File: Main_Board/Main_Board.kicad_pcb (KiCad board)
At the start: 2 copper layers, 60 x 50 mm, 26 parts, among them J1 USB_C_Receptacle_USB2.0_16P, J2 Conn_01x04_Pin, J4 Conn_01x03_Pin, J5 Conn_01x03_Pin, Q1 NMOS, U1 DEV-15583, U2 XIAO-ESP32-C3-DIP, U4 NE555D, U5 TPS72101DBVR

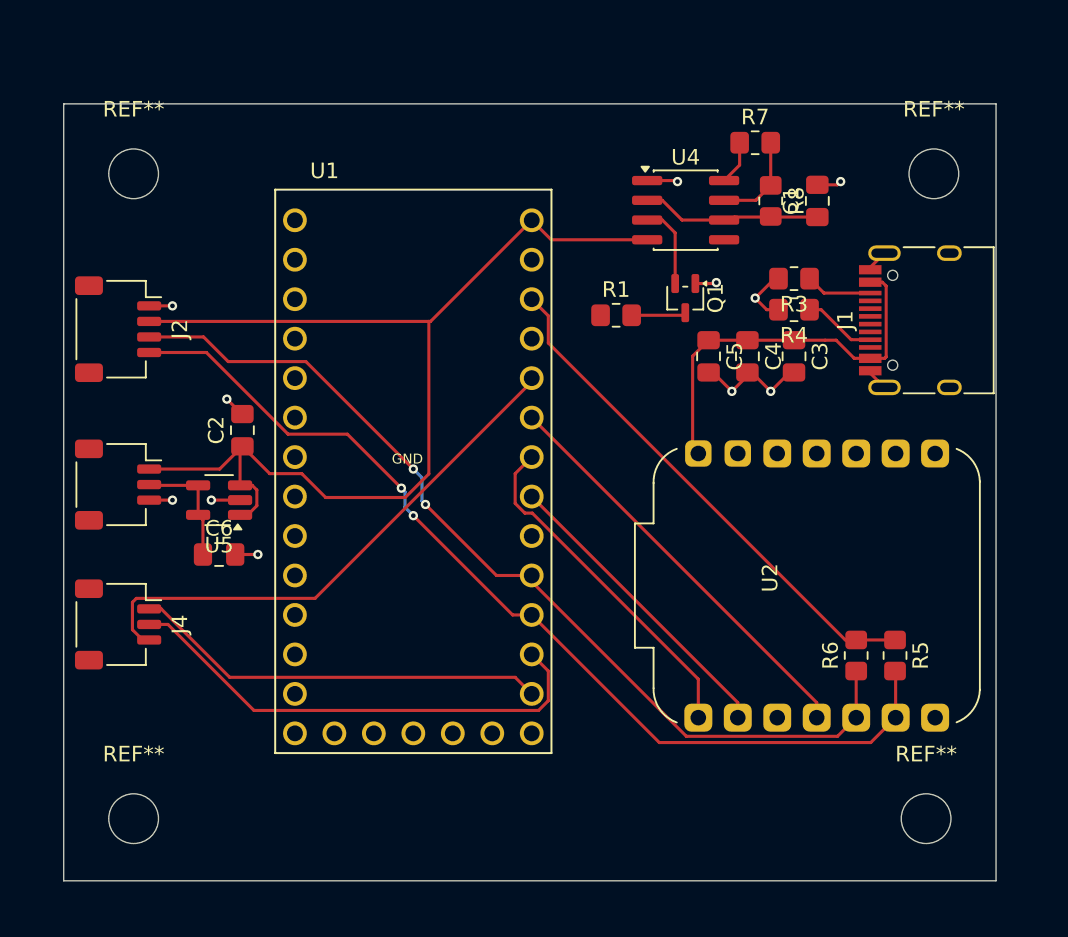
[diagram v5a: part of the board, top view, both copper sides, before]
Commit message: moved mounting holes
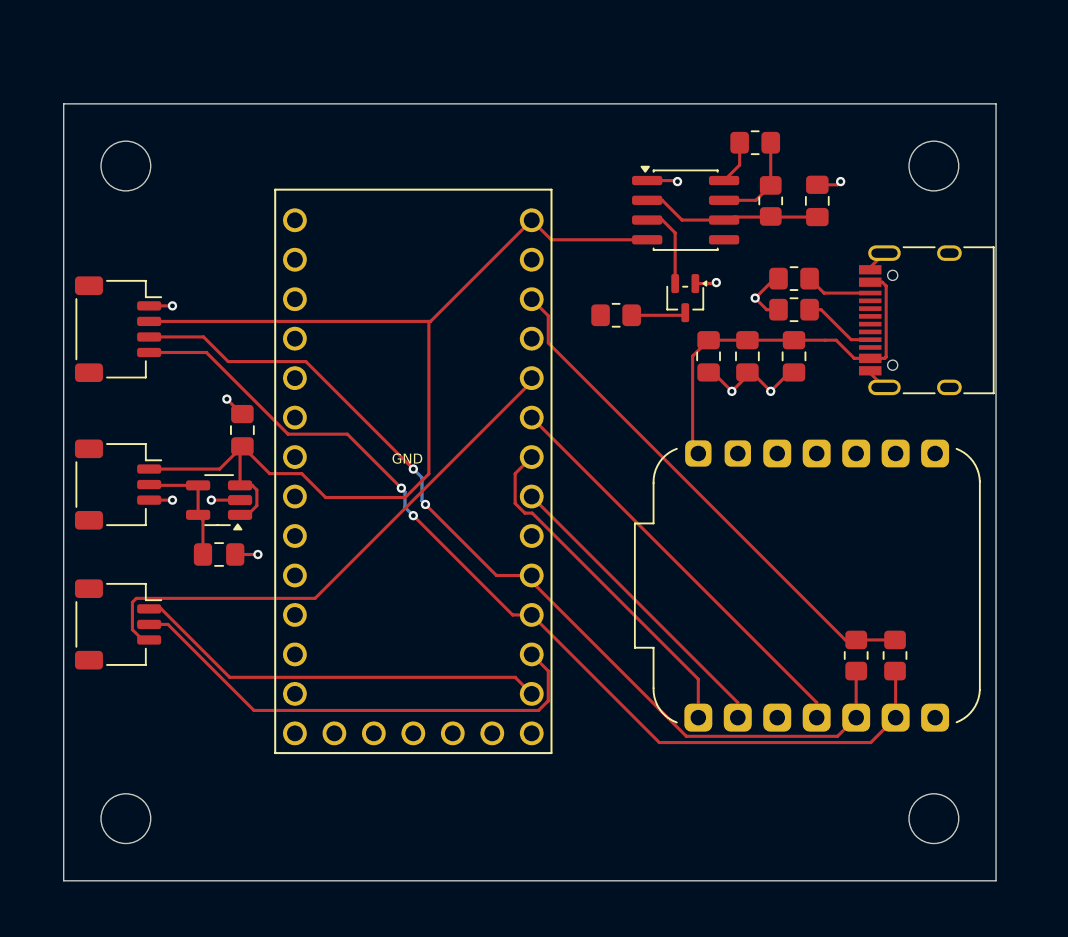
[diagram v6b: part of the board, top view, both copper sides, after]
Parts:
- moved REF** 0.71 mm to (74.0, 79.5)
- moved REF** 0.50 mm to (74.0, 121.5)
- moved REF** 0.50 mm to (126.0, 79.5)
- moved REF** 0.50 mm to (126.0, 121.5)
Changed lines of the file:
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@@
 			(outputformat 1)
 			(mirror no)
-			(drillshape 1)
+			(drillshape 0)
 			(scaleselection 1)
-			(outputdirectory "")
+			(outputdirectory "C:/Users/Maana/Downloads/Feb17_TN_Gerbs/")
 		)
 	)
@@
 			(at 0 -1.68 0)
 			(layer "F.SilkS")
+			(hide yes)
 			(effects
 				(font
@@
 			(at -5.715 -19.685 0)
 			(layer "F.SilkS")
+			(hide yes)
 			(effects
 				(font
@@
 			(at 0 -1.68 90)
 			(layer "F.SilkS")
+			(hide yes)
 			(effects
 				(font
@@
 	(footprint "MountingHole:MountingHole_3.2mm_M3"
 		(layer "F.Cu")
-		(at 74.5 80)
+		(at 74 79.5)
 		(descr "Mounting Hole 3.2mm, M3, no annular, generated by kicad-footprint-generator mountinghole.py")
 		(tags "mountinghole M3")
@@
 			(at 0 -4.15 0)
 			(layer "F.SilkS")
+			(hide yes)
 			(effects
 				(font
@@
 			(at 0 -5.645 90)
 			(layer "F.SilkS")
+			(hide yes)
 			(effects
 				(font
@@
 			(at 0 -1.65 90)
 			(layer "F.SilkS")
+			(hide yes)
 			(effects
 				(font
@@
 			(at 0 -1.65 90)
 			(layer "F.SilkS")
+			(hide yes)
 			(effects
 				(font
@@
 	(footprint "MountingHole:MountingHole_3.2mm_M3"
 		(layer "F.Cu")
-		(at 74.5 121.5)
+		(at 74 121.5)
 		(descr "Mounting Hole 3.2mm, M3, no annular, generated by kicad-footprint-generator mountinghole.py")
 		(tags "mountinghole M3")
@@
 			(at 0 -4.15 0)
 			(layer "F.SilkS")
+			(hide yes)
 			(effects
 				(font
@@
 			(unlocked yes)
 			(layer "F.SilkS")
+			(hide yes)
 			(effects
 				(font
@@
 			(at 0 -2.9 0)
 			(layer "F.SilkS")
+			(hide yes)
 			(effects
 				(font
@@
 			(at 0 -3.98 90)
 			(layer "F.SilkS")
+			(hide yes)
 			(effects
 				(font
@@
 			(at 0 -3.4 0)
 			(layer "F.SilkS")
+			(hide yes)
 			(effects
 				(font
@@
 			(at 0 -3.98 90)
 			(layer "F.SilkS")
+			(hide yes)
 			(effects
 				(font
@@
 			(at 0 -1.65 0)
 			(layer "F.SilkS")
+			(hide yes)
 			(effects
 				(font
@@
 			(at 0 -1.68 90)
 			(layer "F.SilkS")
+			(hide yes)
 			(effects
 				(font
@@
 			(at 0 -1.68 90)
 			(layer "F.SilkS")
+			(hide yes)
 			(effects
 				(font
@@
 			(at 0 -1.65 0)
 			(layer "F.SilkS")
+			(hide yes)
 			(effects
 				(font
@@
 			(at 0 -1.65 0)
 			(layer "F.SilkS")
+			(hide yes)
 			(effects
 				(font
@@
 	(footprint "MountingHole:MountingHole_3.2mm_M3"
 		(layer "F.Cu")
-		(at 126 80)
+		(at 126 79.5)
 		(descr "Mounting Hole 3.2mm, M3, no annular, generated by kicad-footprint-generator mountinghole.py")
 		(tags "mountinghole M3")
@@
 			(at 0 -4.15 0)
 			(layer "F.SilkS")
+			(hide yes)
 			(effects
 				(font
@@
 	(footprint "MountingHole:MountingHole_3.2mm_M3"
 		(layer "F.Cu")
-		(at 125.5 121.5)
+		(at 126 121.5)
 		(descr "Mounting Hole 3.2mm, M3, no annular, generated by kicad-footprint-generator mountinghole.py")
 		(tags "mountinghole M3")
@@
 			(at 0 -4.15 0)
 			(layer "F.SilkS")
+			(hide yes)
 			(effects
 				(font
@@
 			(at 0 -1.68 90)
 			(layer "F.SilkS")
+			(hide yes)
 			(effects
 				(font
@@
 			(at 0 -1.65 90)
 			(layer "F.SilkS")
+			(hide yes)
 			(effects
 				(font
@@
 			(at 0 -1.65 0)
 			(layer "F.SilkS")
+			(hide yes)
 			(effects
 				(font
@@
 			(at 0 -1.95 90)
 			(layer "F.SilkS")
+			(hide yes)
 			(effects
 				(font
@@
 			(at 0 -1.68 90)
 			(layer "F.SilkS")
+			(hide yes)
 			(effects
 				(font
